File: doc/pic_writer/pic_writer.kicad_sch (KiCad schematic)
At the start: 17 parts, among them J1 Conn_01x05, J2 Conn_01x03, Q1 2SB631, Q2 2SC1815, T1 100v 9v, U1 ESP32-C3, U2 LT1963AxST-1.8

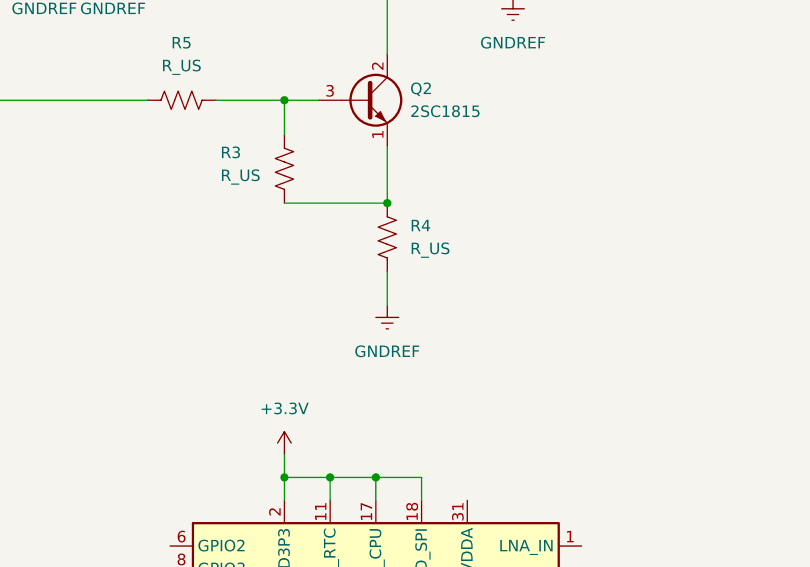
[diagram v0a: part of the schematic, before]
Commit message: fixed npn emitter
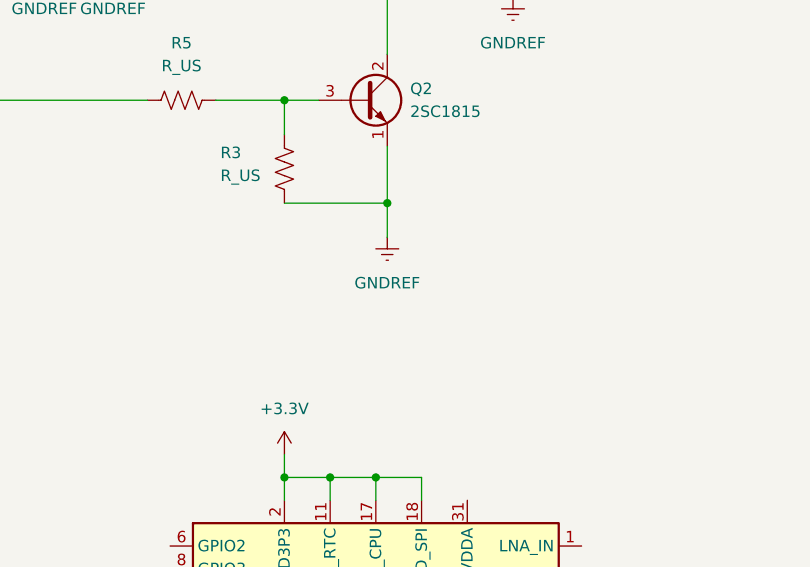
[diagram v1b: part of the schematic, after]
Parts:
- removed R4: R_US, symbol Device:R_US
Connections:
- net GNDREF: now also Q2.1 (E), R3.2
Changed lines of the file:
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@@
 	(wire
 		(pts
-			(xy 128.27 82.55) (xy 128.27 86.36)
+			(xy 128.27 74.93) (xy 128.27 78.74)
 		)
 		(stroke
@@
 	(symbol
 		(lib_id "power:GNDREF")
-		(at 128.27 86.36 0)
+		(at 128.27 78.74 0)
 		(unit 1)
 		(exclude_from_sim no)
@@
 		(fields_autoplaced yes)
 		(property "Reference" "#PWR04"
-			(at 128.27 92.71 0)
+			(at 128.27 85.09 0)
 			(effects
 				(font
@@
 		)
 		(property "Value" "GNDREF"
-			(at 128.27 91.44 0)
+			(at 128.27 83.82 0)
 			(effects
 				(font
@@
 		)
 		(property "Footprint" ""
-			(at 128.27 86.36 0)
+			(at 128.27 78.74 0)
 			(effects
 				(font
@@
 		)
 		(property "Datasheet" ""
-			(at 128.27 86.36 0)
+			(at 128.27 78.74 0)
 			(effects
 				(font
@@
 		)
 		(property "Description" "Power symbol creates a global label with name \"GNDREF\" , reference supply ground"
-			(at 128.27 86.36 0)
+			(at 128.27 78.74 0)
 			(effects
 				(font
@@
 					(unit 1)
 				)
-			)
-		)
-	)
-	(symbol
-		(lib_id "Device:R_US")
-		(at 128.27 78.74 0)
-		(unit 1)
-		(exclude_from_sim no)
-		(in_bom yes)
-		(on_board yes)
-		(dnp no)
-		(fields_autoplaced yes)
-		(property "Reference" "R4"
-			(at 130.81 77.4699 0)
-			(effects
-				(font
-					(size 1.27 1.27)
-				)
-				(justify left)
-			)
-		)
-		(property "Value" "R_US"
-			(at 130.81 80.0099 0)
-			(effects
-				(font
-					(size 1.27 1.27)
-				)
-				(justify left)
-			)
-		)
-		(property "Footprint" ""
-			(at 129.286 78.994 90)
-			(effects
-				(font
-					(size 1.27 1.27)
-				)
-				(hide yes)
-			)
-		)
-		(property "Datasheet" "~"
-			(at 128.27 78.74 0)
-			(effects
-				(font
-					(size 1.27 1.27)
-				)
-				(hide yes)
-			)
-		)
-		(property "Description" "Resistor, US symbol"
-			(at 128.27 78.74 0)
-			(effects
-				(font
-					(size 1.27 1.27)
-				)
-				(hide yes)
-			)
-		)
-		(pin "1"
-		)
-		(pin "2"
-		)
-		(instances
-			(project ""
-				(path "/97f72a07-973a-4672-98cd-d50a7c39c47d"
-					(reference "R4")
-					(unit 1)
-				)

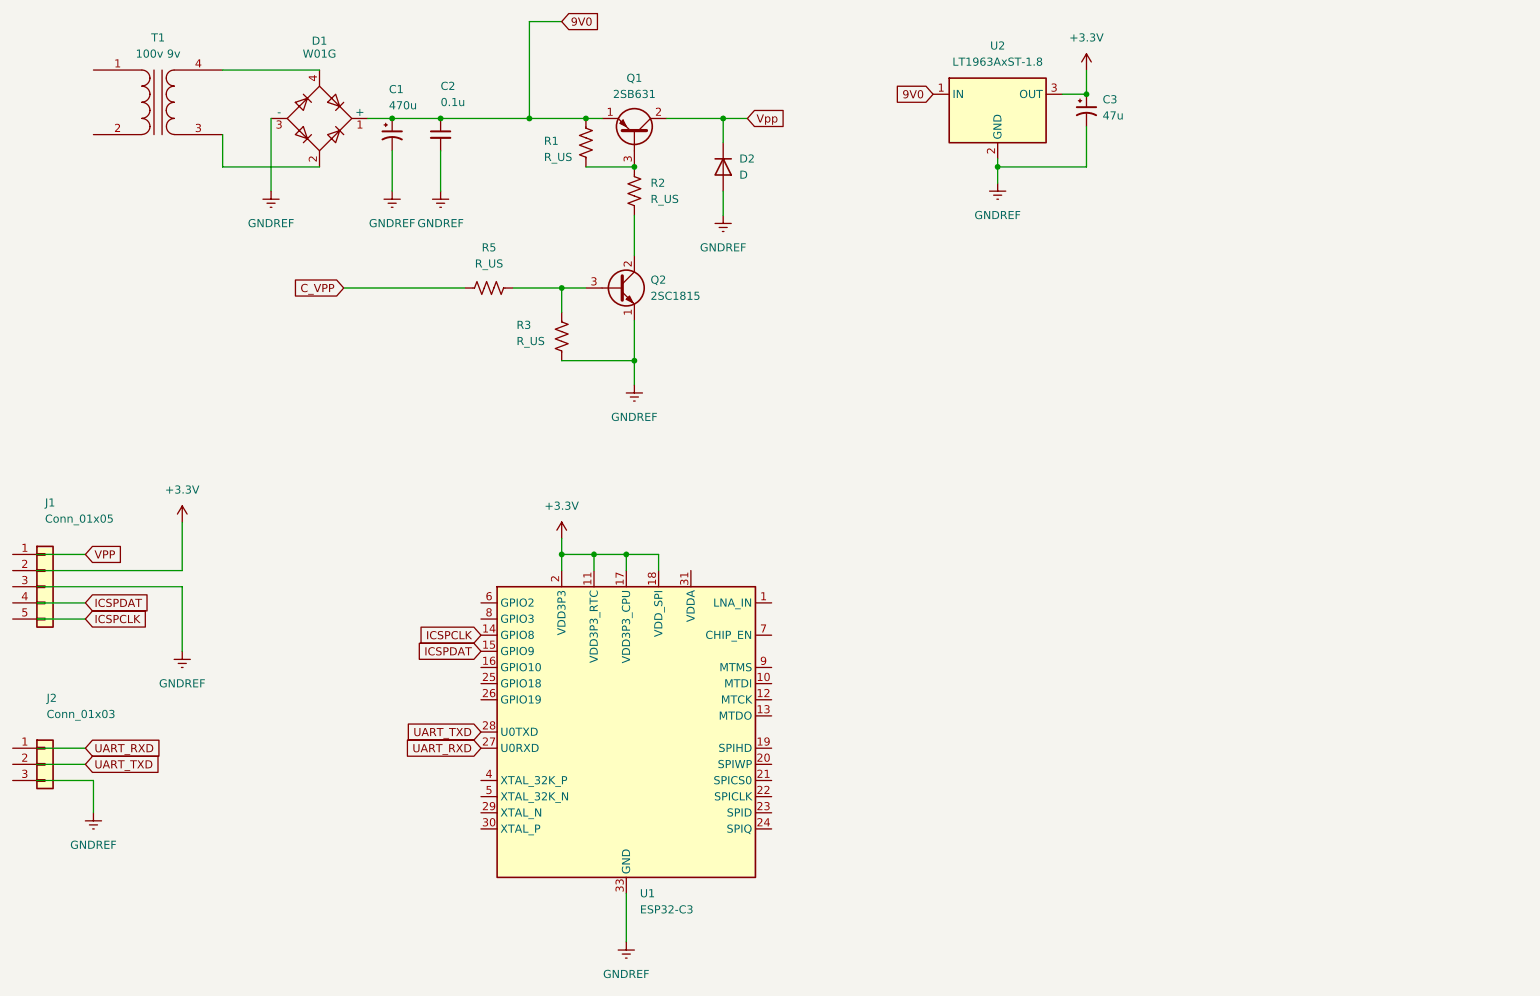
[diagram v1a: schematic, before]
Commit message: add vdd control
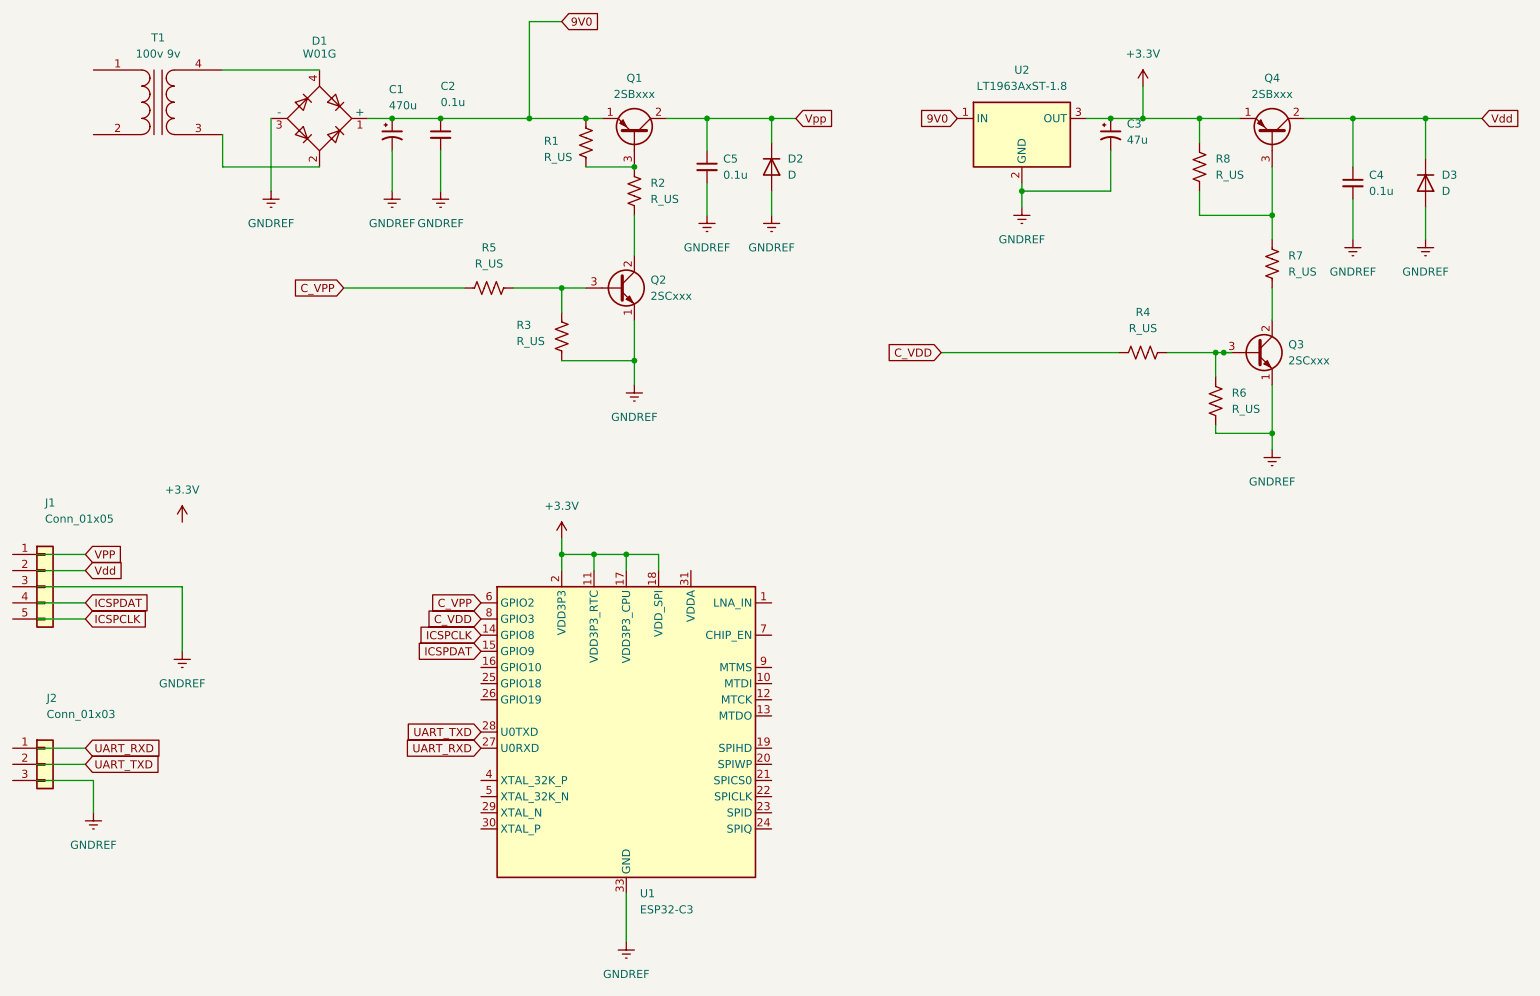
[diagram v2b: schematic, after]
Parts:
- added C4, C5: 0.1u, symbol Device:C_Small
- added D3: D, symbol Device:D
- added Q3: 2SCxxx, Package_TO_SOT_THT:TO-92_Inline, symbol Transistor_BJT:2SC1815
- added Q4: 2SBxxx, Package_TO_SOT_THT:TO-126-3_Vertical, symbol Transistor_BJT:2SB631
- added R4, R6, R7, R8: R_US, symbol Device:R_US
- Q1: value 2SB631 -> 2SBxxx
- Q2: value 2SC1815 -> 2SCxxx
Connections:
- net +3.3V: now also Q4.1 (E), R8.1
- net C_VPP: now also U1.6 (GPIO2)
- net GNDREF: now also C4.2, C5.2, D3.2 (A), Q3.1 (E), R6.2
- net Vpp: now also C5.1
- net C_VDD: now reaches U1.8 (GPIO3)
- net C_VDD: now also R4.1
- new net: Q3.2 (C), R7.2
- new net: Q3.3 (B), R4.2, R6.1
- new net: Q4.3 (B), R7.1, R8.2
- new net Vdd: C4.1, D3.1 (K), Q4.2 (C)
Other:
- moved on the sheet: C3, D2, U2
